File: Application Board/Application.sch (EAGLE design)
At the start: 54 parts, among them Q1 DMP2012SN-7, T1 FDN340P, T2 AP1117_LIN_REG, U1 LM3409HV'LM3409HV', X1 22-23-2101

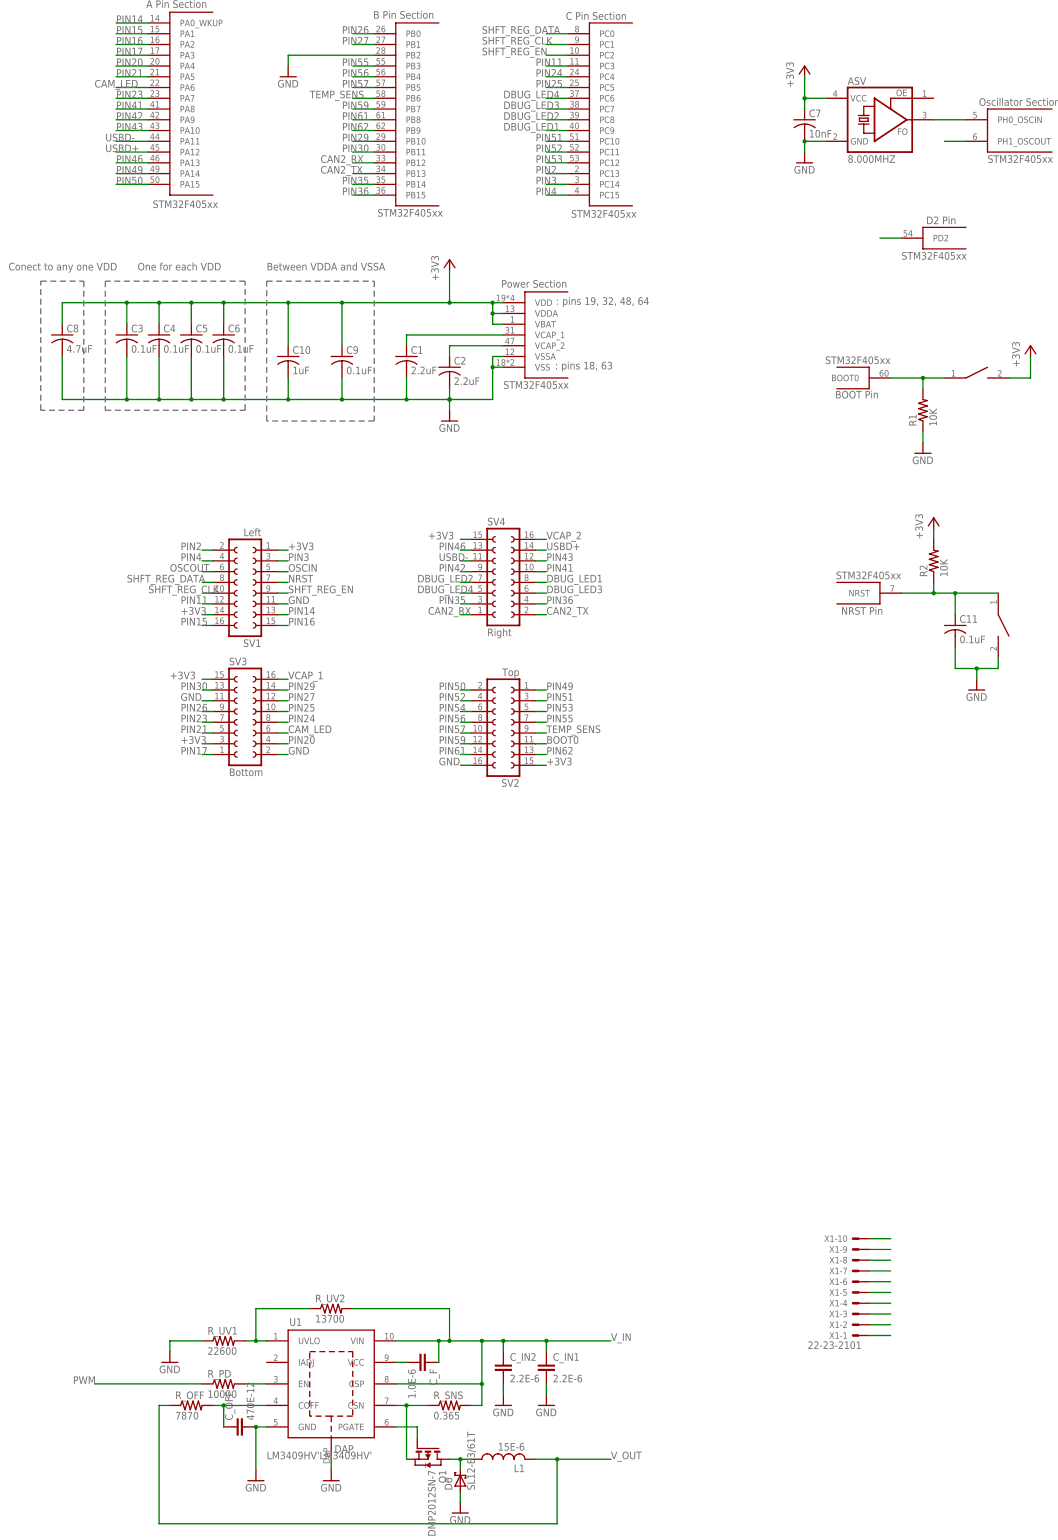
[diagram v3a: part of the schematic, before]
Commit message: Rearranged components, including LED driver.
Not finished, still need to fix LED driver and route the remaining
connector lines.
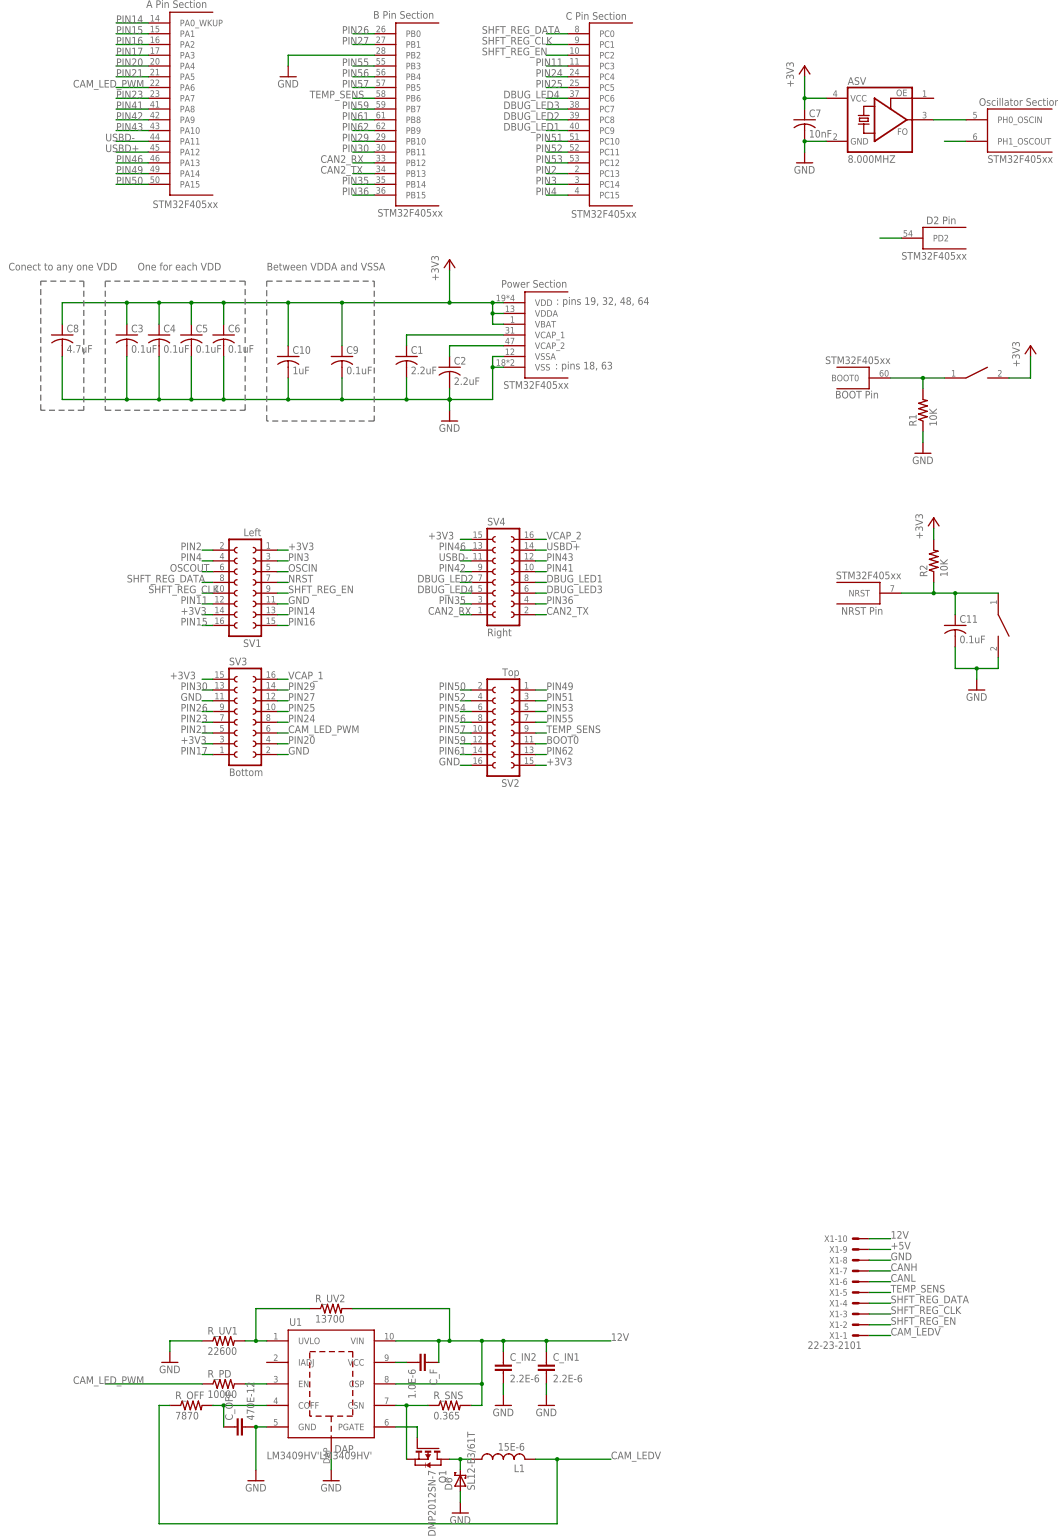
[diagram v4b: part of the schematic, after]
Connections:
- removed net CAM_LED: SV3.6, U$1G$1.PA6, X1-1.S
- removed net PWM: R_PD.1
- removed net V_IN: C_F.1, C_IN1.1, C_IN2.1, R_SNS.2, R_UV2.2, U1.CSP, U1.VIN
- removed net V_OUT: L1.2, R_OFF.1
- new net CAM_LEDV: L1.2, R_OFF.1, X1-1.S
- new net CAM_LED_PWM: R_PD.1, SV3.6, U$1G$1.PA6
- net 12V: now also C_F.1, C_IN1.1, C_IN2.1, R_SNS.2, R_UV2.2, U1.CSP, U1.VIN

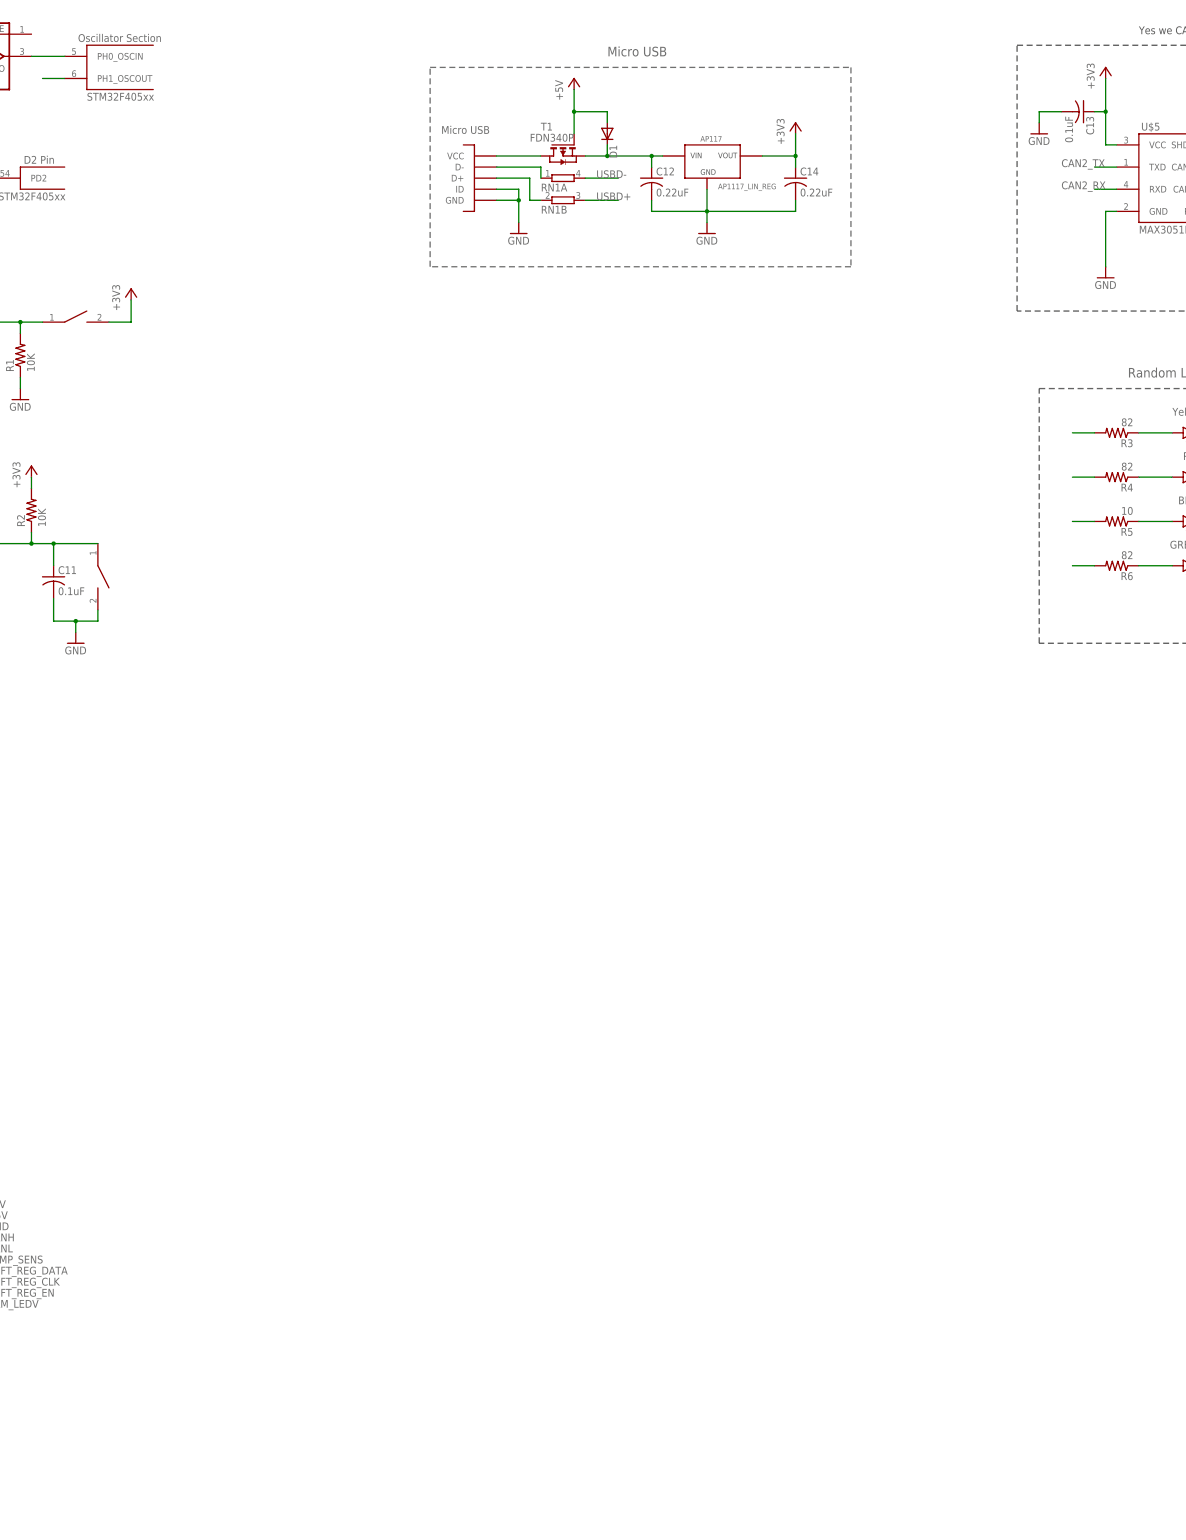
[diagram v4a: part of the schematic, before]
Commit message: updated stm... microcontroller to the updated version
organized order of output lines. Still not complete.
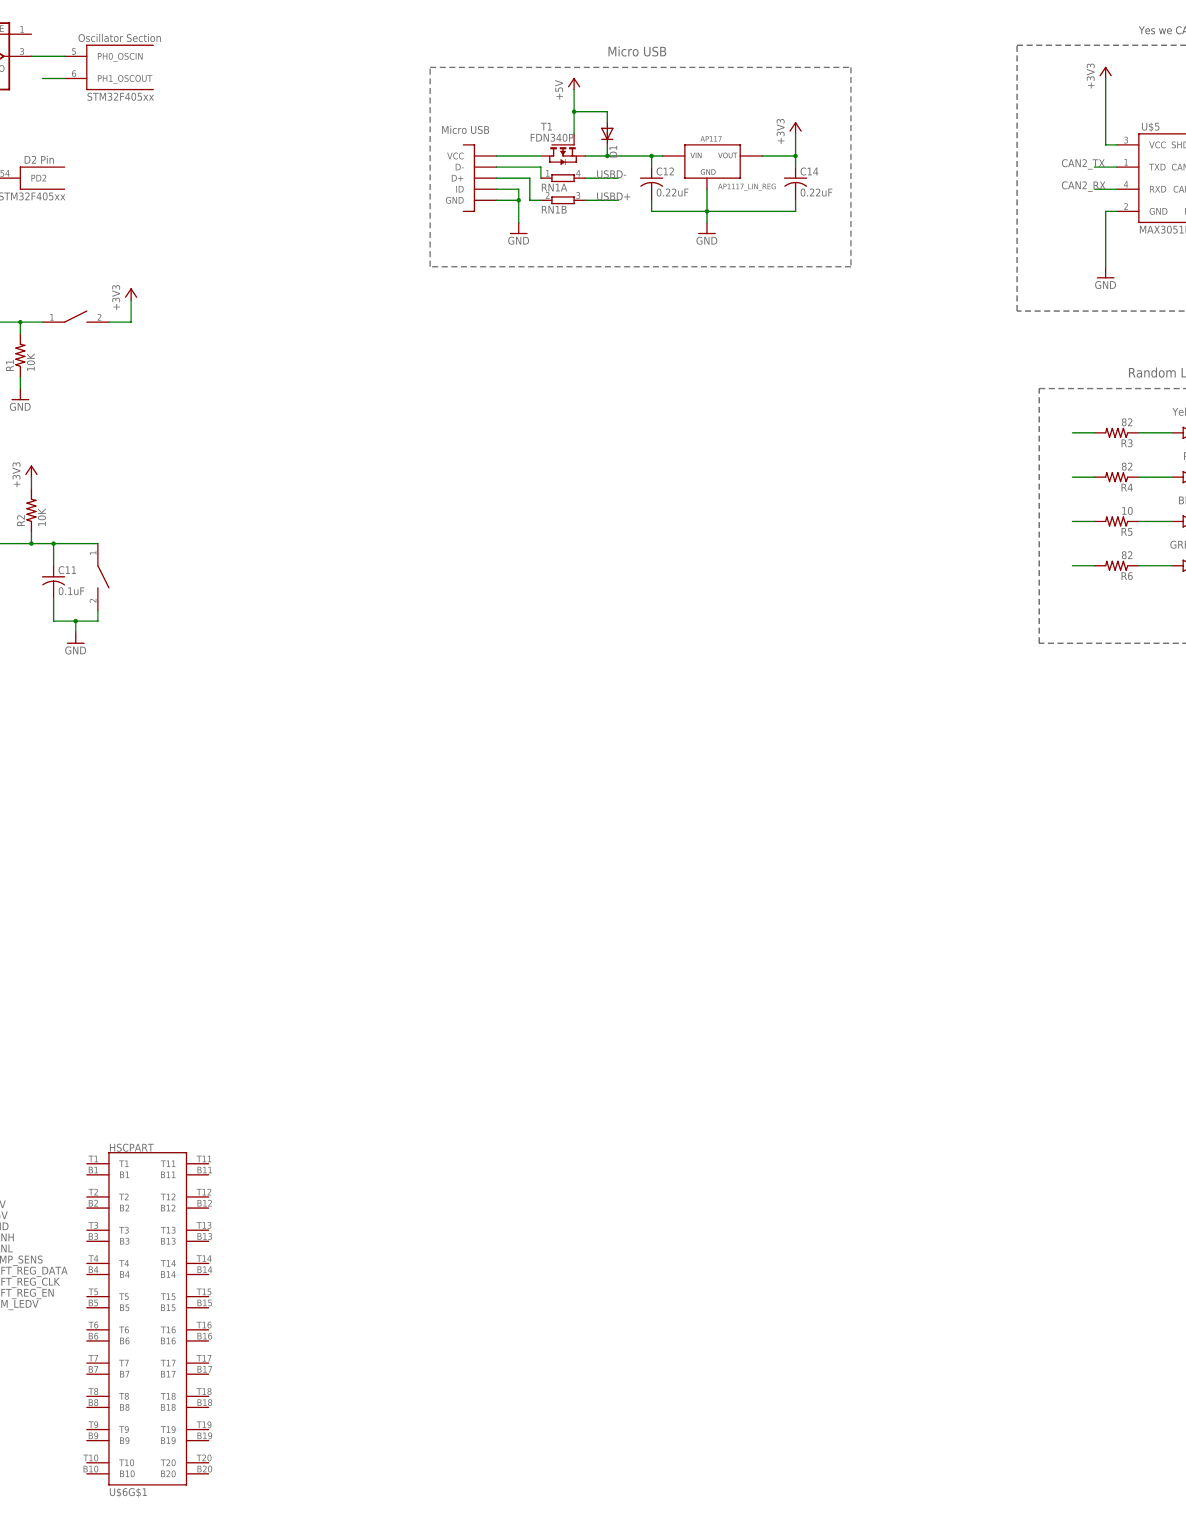
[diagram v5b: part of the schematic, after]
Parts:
- removed C13: 0.1uF, rcl:C-USC0603
- added U$6: HSCPART, Connectors:HSCPART
- renumbered U$2 to S1, U$3 to S2
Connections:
- net +3V3: no longer C13.1
- net GND: no longer C13.2
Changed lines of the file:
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@@
 <part name="C11" library="rcl" deviceset="C-US" device="C0603" value="0.1uF"/>
 <part name="GND2" library="supply1" deviceset="GND" device=""/>
-<part name="U$2" library="DiscreteComponents" deviceset="SWITCH" device=""/>
+<part name="S1" library="DiscreteComponents" deviceset="SWITCH" device=""/>
 <part name="U$1" library="Other" deviceset="STM32F405" device=""/>
-<part name="U$3" library="DiscreteComponents" deviceset="SWITCH" device=""/>
+<part name="S2" library="DiscreteComponents" deviceset="SWITCH" device=""/>
 <part name="R1" library="rcl" deviceset="R-US_" device="R0603" value="10K"/>
 <part name="R2" library="rcl" deviceset="R-US_" device="R0603" value="10K"/>
@@
 <part name="GND8" library="SparkFun-Aesthetics" deviceset="GND" device=""/>
 <part name="GND9" library="SparkFun-Aesthetics" deviceset="GND" device=""/>
-<part name="GND10" library="SparkFun-Aesthetics" deviceset="GND" device=""/>
 <part name="+3V6" library="supply1" deviceset="+3V3" device=""/>
 <part name="R13" library="rcl" deviceset="R-US_" device="R0603" value="120"/>
 <part name="R14" library="rcl" deviceset="R-US_" device="R0603" value="100K"/>
-<part name="C13" library="rcl" deviceset="C-US" device="C0603" value="0.1uF"/>
 <part name="T2" library="PowerComponents" deviceset="AP1117_LIN_REG" device=""/>
 <part name="C12" library="rcl" deviceset="C-US" device="C0603" value="0.22uF"/>
@@
 <part name="FRAME3" library="frames" deviceset="FRAME_A_L" device=""/>
 <part name="X1" library="con-molex" deviceset="22-23-2101" device=""/>
+<part name="U$6" library="Connectors" deviceset="HSCPART" device=""/>
 </parts>
 <sheets>
@@
 <instance part="C11" gate="G$1" x="203.2" y="45.72"/>
 <instance part="GND2" gate="1" x="167.64" y="154.94"/>
-<instance part="U$2" gate="G$1" x="208.28" y="104.14"/>
+<instance part="S1" gate="G$1" x="208.28" y="104.14"/>
 <instance part="U$1" gate="G$1" x="25.4" y="167.64"/>
 <instance part="U$1" gate="G$2" x="78.74" y="165.1"/>
@@
 <instance part="U$1" gate="G$7" x="220.98" y="162.56"/>
 <instance part="U$1" gate="G$8" x="203.2" y="137.16"/>
-<instance part="U$3" gate="G$1" x="213.36" y="45.72" rot="R270"/>
+<instance part="S2" gate="G$1" x="213.36" y="45.72" rot="R270"/>
 <instance part="R1" gate="G$1" x="195.58" y="96.52" rot="R90"/>
 <instance part="R2" gate="G$1" x="198.12" y="60.96" rot="R90"/>
@@
 <instance part="GND8" gate="1" x="444.5" y="114.3"/>
 <instance part="GND9" gate="1" x="487.68" y="124.46"/>
-<instance part="GND10" gate="1" x="429.26" y="147.32"/>
 <instance part="+3V6" gate="G$1" x="444.5" y="162.56"/>
 <instance part="R13" gate="G$1" x="482.6" y="139.7" rot="R270"/>
 <instance part="R14" gate="G$1" x="480.06" y="129.54"/>
-<instance part="C13" gate="G$1" x="439.42" y="152.4" rot="R270"/>
 <instance part="T2" gate="G$1" x="353.06" y="139.7"/>
 <instance part="C12" gate="G$1" x="340.36" y="137.16"/>
@@
 <instance part="X1" gate="-9" x="180.34" y="-101.6" rot="R180"/>
 <instance part="X1" gate="-10" x="180.34" y="-99.06" rot="R180"/>
+<instance part="U$6" gate="G$1" x="223.52" y="-111.76"/>
 </instances>
 <busses>
@@
 </segment>
 <segment>
-<pinref part="U$3" gate="G$1" pin="P$2"/>
+<pinref part="S2" gate="G$1" pin="P$2"/>
 <wire x1="213.36" y1="38.1" x2="213.36" y2="35.56" width="0.1524" layer="91"/>
 <pinref part="C11" gate="G$1" pin="2"/>
@@
 </segment>
 <segment>
-<pinref part="GND10" gate="1" pin="GND"/>
-<wire x1="434.34" y1="152.4" x2="429.26" y2="152.4" width="0.1524" layer="91"/>
-<wire x1="429.26" y1="152.4" x2="429.26" y2="149.86" width="0.1524" layer="91"/>
-<pinref part="C13" gate="G$1" pin="2"/>
-</segment>
-<segment>
 <pinref part="R14" gate="G$1" pin="2"/>
 <pinref part="GND9" gate="1" pin="GND"/>
@@
 <segment>
 <pinref part="U$1" gate="G$6" pin="NRST"/>
-<pinref part="U$3" gate="G$1" pin="P$1"/>
+<pinref part="S2" gate="G$1" pin="P$1"/>
 <wire x1="190.5" y1="53.34" x2="198.12" y2="53.34" width="0.1524" layer="91"/>
 <pinref part="R2" gate="G$1" pin="1"/>
@@
 <segment>
 <pinref part="U$1" gate="G$5" pin="BOOT0"/>
-<pinref part="U$2" gate="G$1" pin="P$1"/>
+<pinref part="S1" gate="G$1" pin="P$1"/>
 <wire x1="187.96" y1="104.14" x2="195.58" y2="104.14" width="0.1524" layer="91"/>
 <pinref part="R1" gate="G$1" pin="2"/>
@@
 </segment>
 <segment>
-<pinref part="U$2" gate="G$1" pin="P$2"/>
+<pinref part="S1" gate="G$1" pin="P$2"/>
 <wire x1="215.9" y1="104.14" x2="220.98" y2="104.14" width="0.1524" layer="91"/>
 <wire x1="220.98" y1="104.14" x2="220.98" y2="109.22" width="0.1524" layer="91"/>
@@
 <wire x1="447.04" y1="144.78" x2="444.5" y2="144.78" width="0.1524" layer="91"/>
 <pinref part="+3V6" gate="G$1" pin="+3V3"/>
-<wire x1="444.5" y1="160.02" x2="444.5" y2="152.4" width="0.1524" layer="91"/>
-<wire x1="444.5" y1="152.4" x2="444.5" y2="144.78" width="0.1524" layer="91"/>
-<wire x1="444.5" y1="152.4" x2="441.96" y2="152.4" width="0.1524" layer="91"/>
-<junction x="444.5" y="152.4"/>
-<pinref part="C13" gate="G$1" pin="1"/>
-</segment>
-<segment>
+<wire x1="444.5" y1="160.02" x2="444.5" y2="144.78" width="0.1524" layer="91"/>
+</segment>
+<segment>
